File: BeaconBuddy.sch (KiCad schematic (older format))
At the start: 32 parts, among them P1 CONN_01X06, P2 AIN0, U1 nRF52832-QFAA, U2 Si7020-A20, U3 BMP280, Y1 32.768kHz, Y2 32MHz

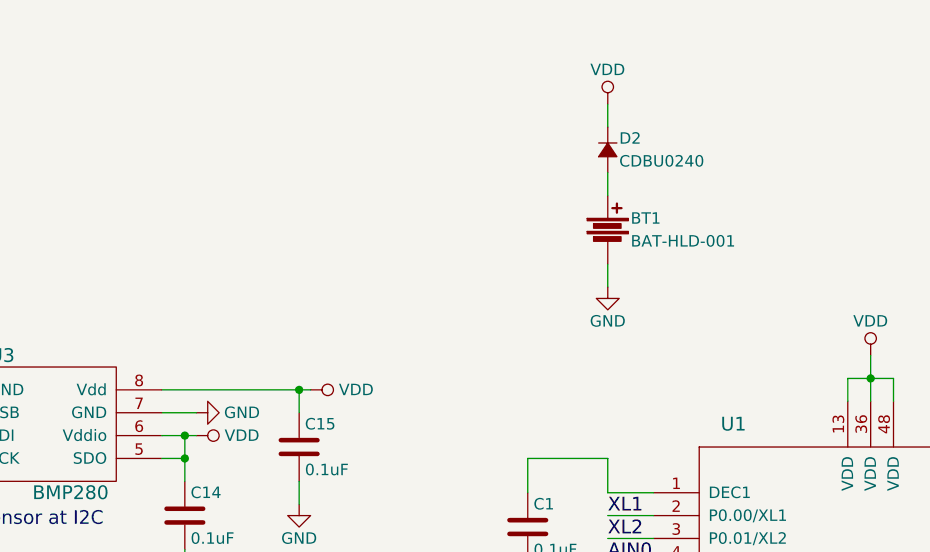
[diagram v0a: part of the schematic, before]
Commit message: Switch to PMOS battery protection
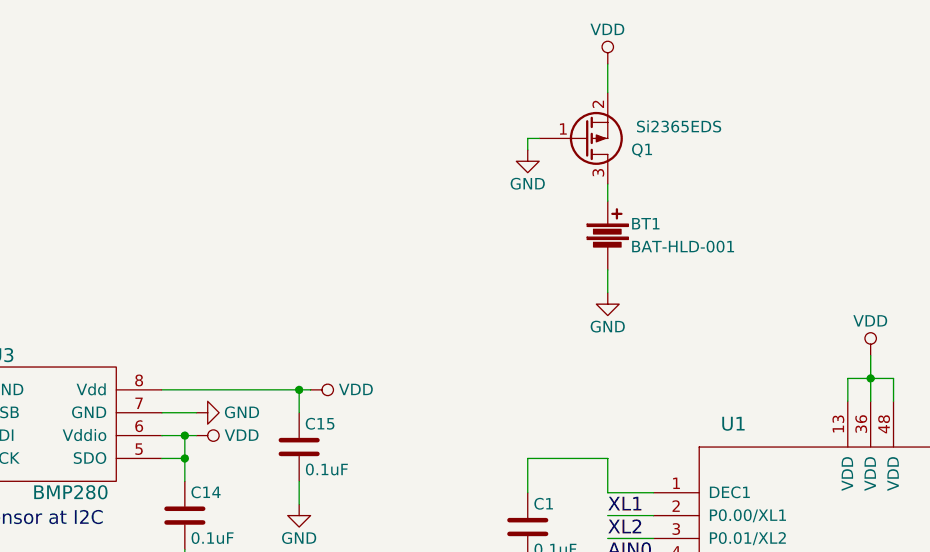
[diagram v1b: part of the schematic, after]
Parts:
- removed D2: CDBU0240, Capacitors_SMD:C_0603, symbol D_Small
- added Q1: Si2365EDS, TO_SOT_Packages_SMD:SOT-23, symbol Q_PMOS_GSD
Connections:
- net GND: now also Q1.1 (G)
- net VDD: now also Q1.2 (S)
- net at BT1.1: now also Q1.3 (D)
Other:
- moved on the sheet: BT1

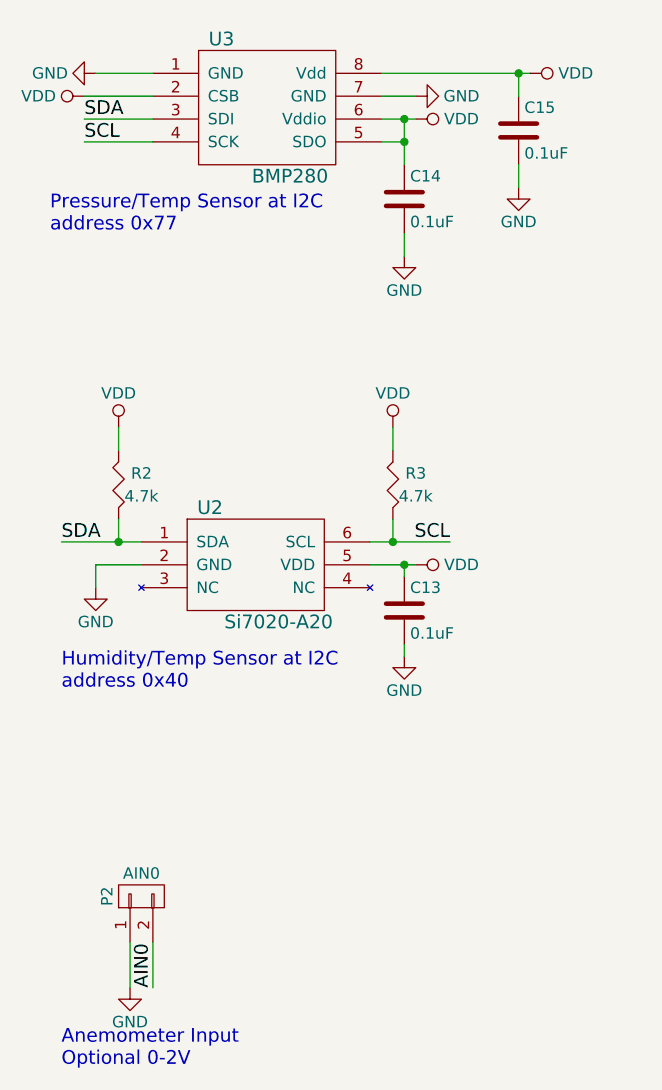
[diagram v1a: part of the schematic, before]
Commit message: Switch to BME280, update PCB
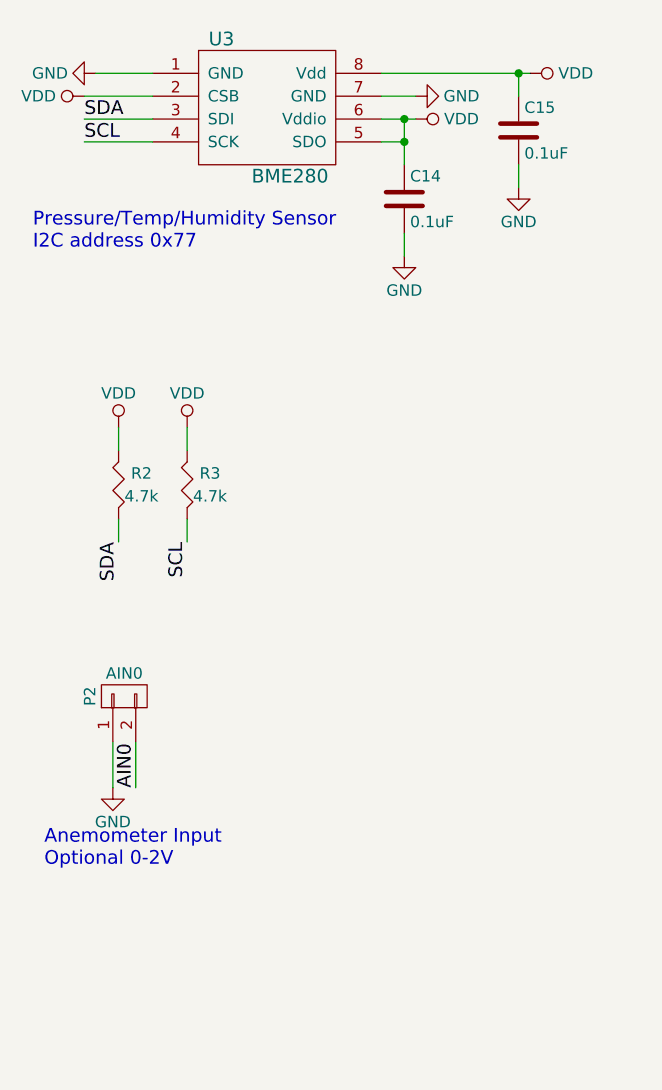
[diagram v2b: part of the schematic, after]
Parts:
- removed C13: 0.1uF, Capacitors_SMD:C_0603, symbol C
- removed U2: Si7020-A20, New_Footprints:S-PWSON-N6, symbol HDC1080
- U3: value BMP280 -> BME280; footprint New_Footprints:Bosch_LGA8 -> new_footprints:Bosch_LGA8_2.5x2.5
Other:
- note added: "Pressure/Temp/Humidity Sensor\nI2C address 0x77"
- note removed: "Humidity/Temp Sensor at I2C\naddress 0x40"
- note removed: "Pressure/Temp Sensor at I2C\naddress 0x77"
- moved on the sheet: P2, R3
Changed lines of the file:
@@
 Wire Wire Line
 	9950 3000 9950 2900
-$Comp
-L HDC1080 U2
-U 1 1 5789A474
-P 1850 4400
-F 0 "U2" H 1650 4650 60  0000 C CNN
-F 1 "Si7020-A20" H 1950 4150 60  0000 C CNN
-F 2 "New_Footprints:S-PWSON-N6" H 1850 4400 60  0001 C CNN
-F 3 "" H 1850 4400 60  0000 C CNN
-	1    1850 4400
-	1    0    0    -1
-$EndComp
 Wire Wire Line
 	4550 3400 4350 3400
@@
 Text Label 4350 3500 0    60   ~ 0
 SCL
-Wire Wire Line
-	2350 4300 2700 4300
-Wire Wire Line
-	1000 4300 1350 4300
-Text Label 1000 4300 0    60   ~ 0
+Text Label 1250 4300 3    60   ~ 0
 SDA
-Text Label 2700 4300 2    60   ~ 0
+Text Label 1550 4300 3    60   ~ 0
 SCL
-Wire Wire Line
-	1350 4400 1150 4400
-Wire Wire Line
-	1150 4400 1150 4500
-Wire Wire Line
-	2350 4400 2550 4400
-$Comp
-L GND #PWR3
-U 1 1 5789B2A5
-P 1150 4500
-F 0 "#PWR3" H 1150 4250 50  0001 C CNN
-F 1 "GND" H 1150 4350 50  0000 C CNN
-F 2 "" H 1150 4500 50  0000 C CNN
-F 3 "" H 1150 4500 50  0000 C CNN
-	1    1150 4500
-	1    0    0    -1
-$EndComp
-$Comp
-L VDD #PWR11
-U 1 1 5789B35F
-P 2550 4400
-F 0 "#PWR11" H 2550 4250 50  0001 C CNN
-F 1 "VDD" V 2550 4600 50  0000 C CNN
-F 2 "" H 2550 4400 50  0000 C CNN
-F 3 "" H 2550 4400 50  0000 C CNN
-	1    2550 4400
-	0    1    1    0
-$EndComp
 $Comp
 L R R3
 U 1 1 5789BB3A
-P 2450 4050
-F 0 "R3" H 2550 4100 50  0000 C CNN
-F 1 "4.7k" H 2550 4000 50  0000 C CNN
-F 2 "Resistors_SMD:R_0603" V 2380 4050 30  0001 C CNN
-F 3 "" H 2450 4050 30  0000 C CNN
-	1    2450 4050
+P 1550 4050
+F 0 "R3" H 1650 4100 50  0000 C CNN
+F 1 "4.7k" H 1650 4000 50  0000 C CNN
+F 2 "Resistors_SMD:R_0603" V 1480 4050 30  0001 C CNN
+F 3 "" H 1550 4050 30  0000 C CNN
+	1    1550 4050
 	1    0    0    -1
 $EndComp
@@
 $EndComp
 Wire Wire Line
-	2450 4200 2450 4300
-Connection ~ 2450 4300
+	1550 4200 1550 4300
 Wire Wire Line
 	1250 4200 1250 4300
-Connection ~ 1250 4300
 Wire Wire Line
 	1250 3900 1250 3800
 Wire Wire Line
-	2450 3900 2450 3800
+	1550 3900 1550 3800
 $Comp
 L VDD #PWR6
 U 1 1 5789C043
-P 2450 3800
-F 0 "#PWR6" H 2450 3650 50  0001 C CNN
-F 1 "VDD" H 2450 3950 50  0000 C CNN
-F 2 "" H 2450 3800 50  0000 C CNN
-F 3 "" H 2450 3800 50  0000 C CNN
-	1    2450 3800
+P 1550 3800
+F 0 "#PWR6" H 1550 3650 50  0001 C CNN
+F 1 "VDD" H 1550 3950 50  0000 C CNN
+F 2 "" H 1550 3800 50  0000 C CNN
+F 3 "" H 1550 3800 50  0000 C CNN
+	1    1550 3800
 	1    0    0    -1
 $EndComp
@@
 $EndComp
 $Comp
-L C C13
-U 1 1 5789C3A1
-P 2500 4600
-F 0 "C13" H 2525 4700 50  0000 L CNN
-F 1 "0.1uF" H 2525 4500 50  0000 L CNN
-F 2 "Capacitors_SMD:C_0603" H 2538 4450 50  0001 C CNN
-F 3 "" H 2500 4600 50  0000 C CNN
-	1    2500 4600
-	1    0    0    -1
-$EndComp
-Wire Wire Line
-	2500 4450 2500 4400
-Connection ~ 2500 4400
-$Comp
-L GND #PWR8
-U 1 1 5789C4B4
-P 2500 4800
-F 0 "#PWR8" H 2500 4550 50  0001 C CNN
-F 1 "GND" H 2500 4650 50  0000 C CNN
-F 2 "" H 2500 4800 50  0000 C CNN
-F 3 "" H 2500 4800 50  0000 C CNN
-	1    2500 4800
-	1    0    0    -1
-$EndComp
-Wire Wire Line
-	2500 4800 2500 4750
-Text Notes 1000 4950 0    60   ~ 0
-Humidity/Temp Sensor at I2C\naddress 0x40
-$Comp
 L BMP280 U3
 U 1 1 578A83E7
 P 1900 2400
 F 0 "U3" H 1700 2700 60  0000 C CNN
-F 1 "BMP280" H 2000 2100 60  0000 C CNN
-F 2 "New_Footprints:Bosch_LGA8" H 1900 2400 60  0001 C CNN
+F 1 "BME280" H 2000 2100 60  0000 C CNN
+F 2 "new_footprints:Bosch_LGA8_2.5x2.5" H 1900 2400 60  0001 C CNN
 F 3 "" H 1900 2400 60  0000 C CNN
 	1    1900 2400
@@
 Wire Wire Line
 	3000 2750 3000 2650
-Text Notes 950  2950 0    60   ~ 0
-Pressure/Temp Sensor at I2C\naddress 0x77
+Text Notes 875  3025 0    60   ~ 0
+Pressure/Temp/Humidity Sensor\nI2C address 0x77
 Wire Wire Line
 	3000 2350 3000 2250
@@
 L CONN_01X02 P2
 U 1 1 578ADC29
-P 1350 5850
-F 0 "P2" H 1350 6000 50  0000 C CNN
-F 1 "AIN0" V 1450 5850 50  0000 C CNN
-F 2 "New_Footprints:CONN_100mil_1x2" H 1350 5850 50  0001 C CNN
-F 3 "" H 1350 5850 50  0000 C CNN
-	1    1350 5850
+P 1275 4975
+F 0 "P2" H 1275 5125 50  0000 C CNN
+F 1 "AIN0" V 1375 4975 50  0000 C CNN
+F 2 "New_Footprints:CONN_100mil_1x2" H 1275 4975 50  0001 C CNN
+F 3 "" H 1275 4975 50  0000 C CNN
+	1    1275 4975
 	0    -1   -1   0
 $EndComp
 Wire Wire Line
-	1300 6050 1300 6250
-Wire Wire Line
-	1400 6050 1400 6250
-Text Label 1400 6250 1    60   ~ 0
+	1225 5175 1225 5375
+Wire Wire Line
+	1325 5175 1325 5375
+Text Label 1325 5375 1    60   ~ 0
 AIN0
 $Comp
 L GND #PWR5
 U 1 1 578AE478
-P 1300 6250
-F 0 "#PWR5" H 1300 6000 50  0001 C CNN
-F 1 "GND" H 1300 6100 50  0000 C CNN
-F 2 "" H 1300 6250 50  0000 C CNN
-F 3 "" H 1300 6250 50  0000 C CNN
-	1    1300 6250
-	1    0    0    -1
-$EndComp
-Text Notes 1000 6600 0    60   ~ 0
+P 1225 5375
+F 0 "#PWR5" H 1225 5125 50  0001 C CNN
+F 1 "GND" H 1225 5225 50  0000 C CNN
+F 2 "" H 1225 5375 50  0000 C CNN
+F 3 "" H 1225 5375 50  0000 C CNN
+	1    1225 5375
+	1    0    0    -1
+$EndComp
+Text Notes 925  5725 0    60   ~ 0
 Anemometer Input\nOptional 0-2V
 $Comp
